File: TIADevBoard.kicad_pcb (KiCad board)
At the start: 2 copper layers, 30 parts, among them J1 Screw_Terminal_01x02, J2 Conn_Coaxial, J3 Conn_Coaxial, U1 MC33063AD, U2 OPA2387, U3 ADP3330-3, U4 ADP7183

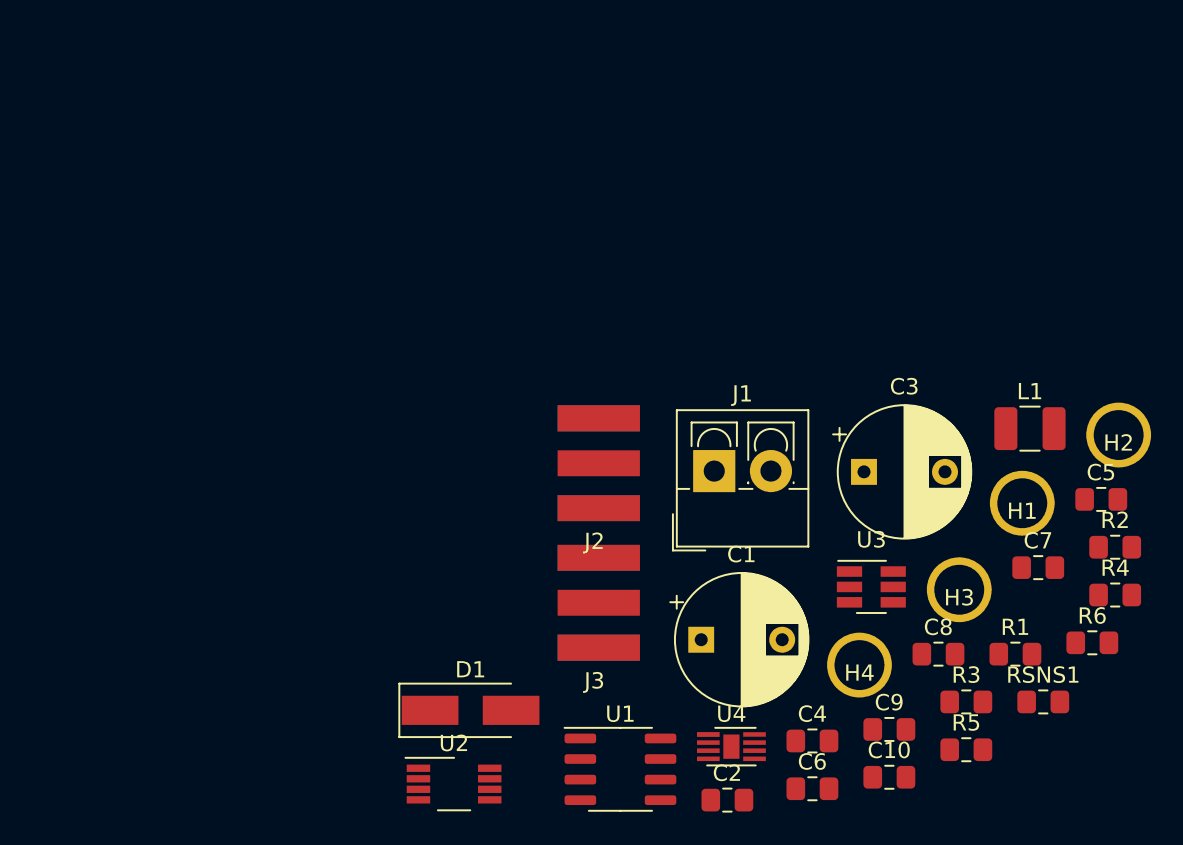
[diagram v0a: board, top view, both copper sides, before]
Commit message: Version 3 complete with +3V/-2.5V low noise LDO regulated supplies, a -5V inverting DC switching converter, and a new low-noise TIA
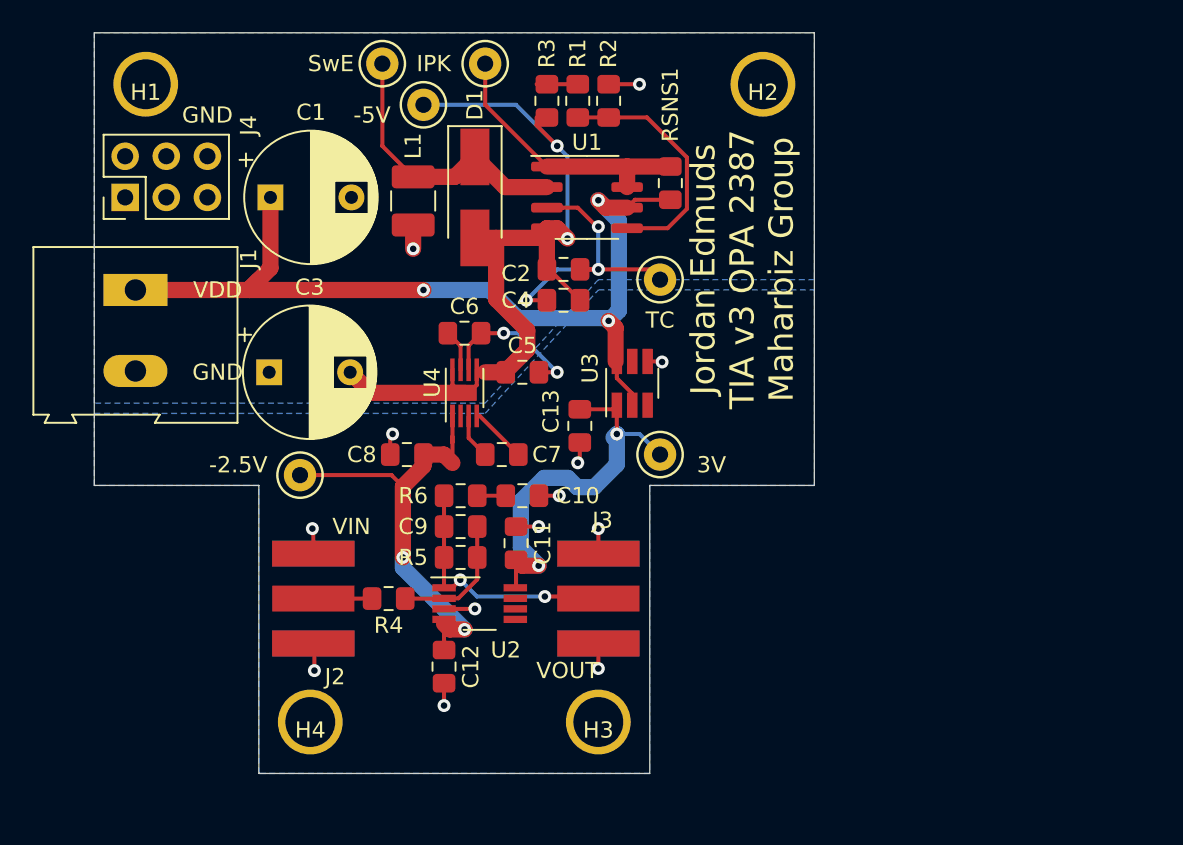
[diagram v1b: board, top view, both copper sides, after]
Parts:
- added C11: 470nF, Capacitor_SMD:C_0805_2012Metric_Pad1.15x1.40mm_HandSolder, F.Cu at (96.5, 98.2)
- added C12: 470nF, Capacitor_SMD:C_0805_2012Metric_Pad1.15x1.40mm_HandSolder, F.Cu at (92.1, 105.8)
- added C13: 10uF, Capacitor_SMD:C_0805_2012Metric_Pad1.15x1.40mm_HandSolder, F.Cu at (100.5, 90.9)
- added J4: Conn_02x03_Counter_Clockwise, Connector_PinHeader_2.54mm:PinHeader_2x03_P2.54mm_Vertical, F.Cu at (72.4, 76.8)
- added TP1: 3V, my_library_foot:TestPoint_Keystone_5000-5004_Miniature, F.Cu at (105.4, 92.7)
- added TP2: IPK, my_library_foot:TestPoint_Keystone_5000-5004_Miniature, F.Cu at (94.6, 68.6)
- added TP3: -5V, my_library_foot:TestPoint_Keystone_5000-5004_Miniature, F.Cu at (90.8, 71.1)
- added TP4: -2.5V, my_library_foot:TestPoint_Keystone_5000-5004_Miniature, F.Cu at (83.2, 94.0)
- added TP5: TC, my_library_foot:TestPoint_Keystone_5000-5004_Miniature, F.Cu at (105.4, 81.9)
- added TP6: SwE, my_library_foot:TestPoint_Keystone_5000-5004_Miniature, F.Cu at (88.3, 68.6)
- J1: footprint TerminalBlock_4Ucon:TerminalBlock_4Ucon_1x02_P3.50mm_Vertical -> TerminalBlock:TerminalBlock_Altech_AK300-2_P5.00mm
- moved H1 60.0 mm to (73.7, 69.8)
- moved R3 45.2 mm to (98.4, 70.9), turned to 90 degrees
- moved R4 44.9 mm to (88.7, 101.6), turned to 180 degrees
- moved R1 43.5 mm to (100.3, 70.9), turned to 270 degrees
- moved R2 41.7 mm to (102.2, 70.9), turned to 90 degrees
- moved L1 40.6 mm to (90.2, 77.1), turned to 270 degrees
- moved R6 40.0 mm to (93.1, 95.2)
- moved RSNS1 39.4 mm to (106.0, 76.0), turned to 270 degrees
- moved C1 38.1 mm to (81.4, 76.8)
- moved J1 37.4 mm to (73.0, 82.5), turned to 270 degrees
- moved C3 37.2 mm to (81.3, 87.6)
- moved C5 36.6 mm to (96.9, 87.6)
- moved C6 35.4 mm to (93.3, 85.2)
- moved U1 35.4 mm to (100.9, 76.8)
- moved C8 35.1 mm to (89.8, 92.7), turned to 180 degrees
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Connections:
- net Net-(C2-Pad1) renamed /TC
- net Net-(C9-Pad1) renamed /VOUT
- net Net-(C9-Pad2) renamed /VOP-
- net Net-(D1-Pad1) renamed /SwE
- net Net-(J2-Pad1) renamed /VIN
- net Net-(R1-Pad2) renamed /VFB
- net Net-(RSNS1-Pad1) renamed /Ipk
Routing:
- net VDD: track 0.00 -> 56.0 mm, vias 0 -> 3
- net -5V: track 0.00 -> 53.8 mm, vias 0 -> 2
- net /-2.5V: track 0.00 -> 28.1 mm, vias 0 -> 2
- net GND: track 0.00 -> 28.0 mm, vias 0 -> 15
- net /3V: track 0.00 -> 24.6 mm, vias 0 -> 2
- net /TC: track 0.00 -> 20.1 mm, vias 0 -> 3
- net /SwE: track 0.00 -> 17.3 mm
- net /Ipk: track 0.00 -> 16.8 mm
- net /VOUT: track 0.00 -> 15.9 mm, vias 0 -> 2
- net /VFB: track 0.00 -> 15.1 mm
- net /VOP-: track 0.00 -> 8.20 mm
- net /VIN: track 0.00 -> 3.62 mm
- net Net-(C7-Pad2): track 0.00 -> 3.56 mm
- net Net-(C7-Pad1): track 0.00 -> 2.81 mm
- net Net-(C6-Pad1): track 0.00 -> 2.58 mm
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- added copper zone on B.Cu, net GND
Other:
- board outline added: 44.5 x 45.7 mm
- board text added: "GND"
- board text added: "Jordan Edmuds TIA v3 OPA 2387 Maharbiz Group"
- board text added: "VDD"
- board text added: "VIN"
- board text added: "VOUT"
